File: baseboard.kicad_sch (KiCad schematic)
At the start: 45 parts, among them J10 AS7265X, J11 TFT_LCD2, J12 SERVO1, J13 USER_GPIO, J14 TFT_LCD, J15 SERVO2, J16 FAN, J17 ADC_IN, J5 Screw_Terminal_01x04, J6 DCMI_CAMERA, J7 LCD_CHAR, J8 UART1, J9 UART2, Q1 BCP56, Q2 BCP56, Q3 BCP56, U2 LM2676S-5, U3 AMS1117-3.3

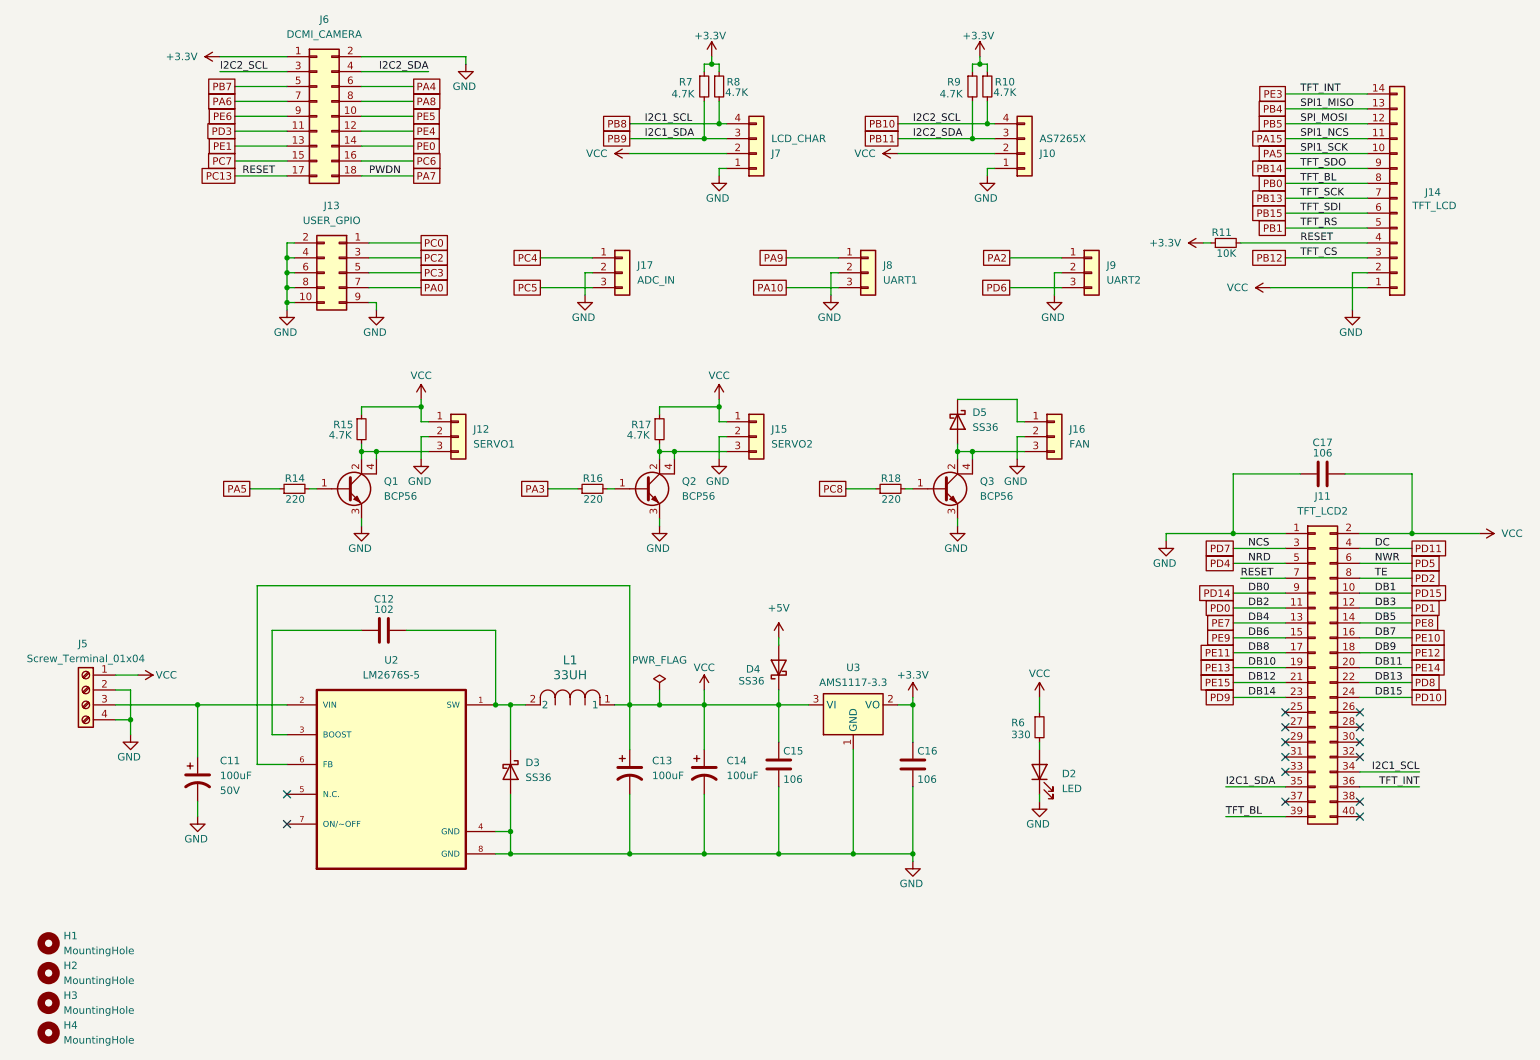
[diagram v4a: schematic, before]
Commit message: flipped camera connector
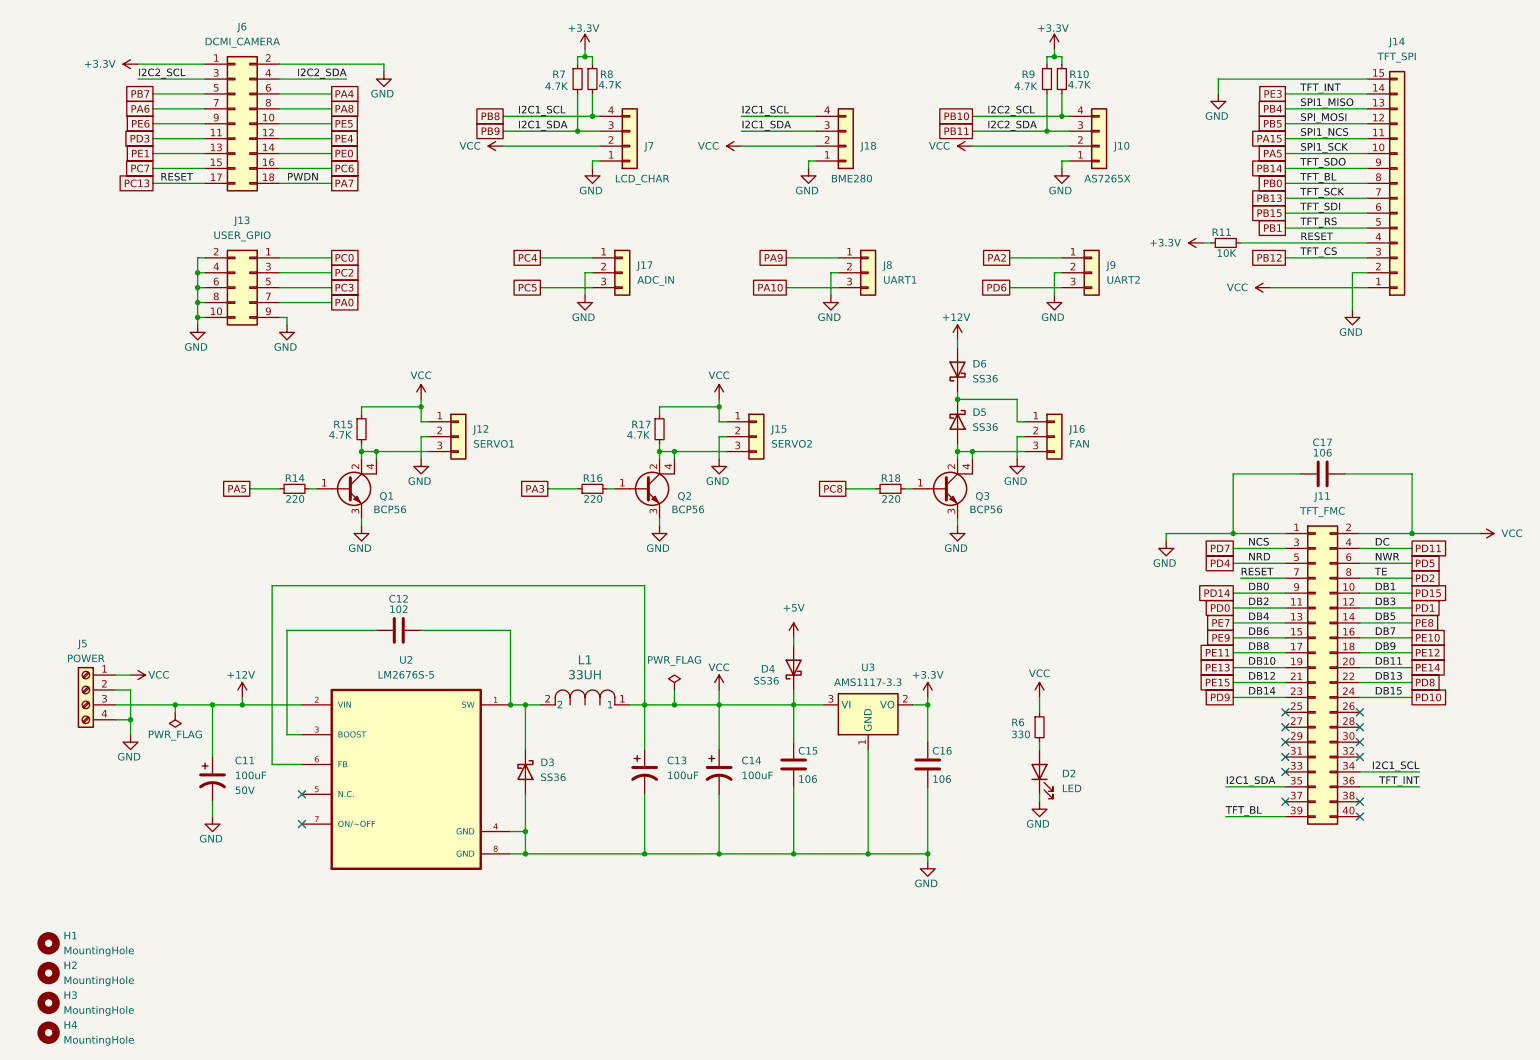
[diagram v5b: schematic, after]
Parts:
- removed J14: TFT_LCD, Connector_PinHeader_2.54mm:PinHeader_1x14_P2.54mm_Vertical, symbol LM2676S-3.3_NOPB:Conn_01x14
- added D6: SS36, Diode_SMD:D_SMA, symbol LM2676S-3.3_NOPB:SS36
- added J14: TFT_SPI, Connector_PinHeader_2.54mm:PinHeader_1x15_P2.54mm_Vertical, symbol Connector_Generic:Conn_01x15
- added J18: BME280, Connector_PinHeader_2.54mm:PinHeader_1x04_P2.54mm_Vertical, symbol LM2676S-3.3_NOPB:Conn_01x04
- D2: footprint LED_THT:LED_D3.0mm -> LED_SMD:LED_0805_2012Metric_Pad1.15x1.40mm_HandSolder
- J11: value TFT_LCD2 -> TFT_FMC
- J5: value Screw_Terminal_01x04 -> POWER
- J6: footprint Connector_PinHeader_2.54mm:PinHeader_2x09_P2.54mm_Vertical -> Connector_PinSocket_2.54mm:PinSocket_2x09_P2.54mm_Vertical
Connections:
- net GND: now also J14.15 (Pin_15), J14.2 (Pin_2), J18.1 (Pin_1)
- net PA15: now also J14.11 (Pin_11)
- net PA5: now also J14.10 (Pin_10)
- net PB0: now also J14.8 (Pin_8)
- net PB1: now also J14.5 (Pin_5)
- net PB12: now also J14.3 (Pin_3)
- net PB13: now also J14.7 (Pin_7)
- net PB14: now also J14.9 (Pin_9)
- net PB15: now also J14.6 (Pin_6)
- net PB4: now also J14.13 (Pin_13)
- net PB5: now also J14.12 (Pin_12)
- net PB8: now also J18.4 (Pin_4)
- net PB9: now also J18.3 (Pin_3)
- net PC13: now also J14.4 (Pin_4)
- net PE3: now also J14.14 (Pin_14)
- net VCC: now also J14.1 (Pin_1), J18.2 (Pin_2)
- net +12V: now reaches C11.1, J5.3 (Pin_3), U2.2 (VIN)
- net +12V: now also D6.2 (A)
- net at D5.1 (K), J16.1 (Pin_1): now also D6.1 (K)
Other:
- moved on the sheet: C11, C12, C13, C14, C15, C16, D3, D4, J10, J13, J6, J7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

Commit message: snapshot
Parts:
- removed H1, H2, H3, H4: MountingHole, MountingHole:MountingHole_3.2mm_M3, symbol LM2676S-3.3_NOPB:MountingHole
- removed Q1, Q2, Q3: BCP56, Package_TO_SOT_SMD:SOT-223-3_TabPin2, symbol Transistor_BJT:BCP56
- added H1, H2, H3, H4: ~, PCM_JLCPCB:Hole, 3mm, symbol PCM_JLCPCB-Manufacturing:Mounting Hole, 3mm, Via Stiched
- added Q1, Q2, Q3: BCP56, PCM_Package_TO_SOT_SMD_AKL:SOT-223-3_TabPin2, symbol PCM_Transistor_BJT_AKL:BCP56
- L1: footprint Inductor_SMD:L_Bourns-SRN8040_8x8.15mm -> JLCPCB:L_SMD,8x8mm
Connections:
- net GND: now also H1.1, H2.1, H3.1, H4.1, Q1.3 (E), Q2.3 (E), Q3.3 (E)
- net at J15.3 (Pin_3), R17.2: now also Q2.2 (C)
- net at D5.2 (A), J16.3 (Pin_3): now also Q3.2 (C)
- net at J12.3 (Pin_3), R15.2: now also Q1.2 (C)
- net at R14.2: now also Q1.1 (B)
- net at R18.2: now also Q3.1 (B)
- net at R16.2: now also Q2.1 (B)

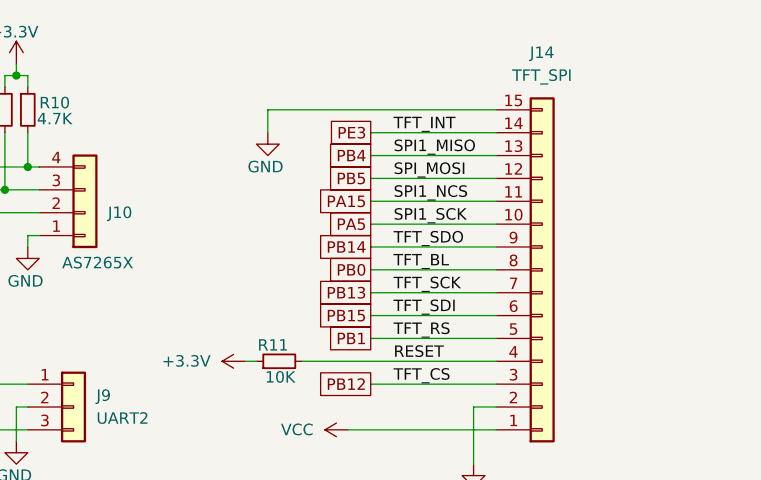
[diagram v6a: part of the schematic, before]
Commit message: Reassign pin (PA5 to PB3) to dix duplicate PA5
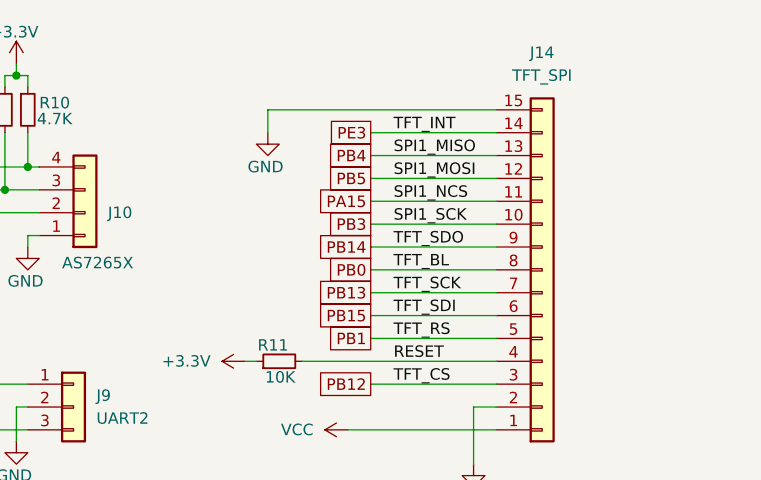
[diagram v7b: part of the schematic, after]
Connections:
- net PA5: no longer J14.10 (Pin_10)
- new net PB3: J14.10 (Pin_10)
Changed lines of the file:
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@@
 		)
 	)
-	(label "SPI_MOSI"
+	(label "SPI1_MOSI"
 		(at 232.41 36.83 0)
 		(effects
@@
 		)
 	)
-	(global_label "PA5"
+	(global_label "PB3"
 		(shape passive)
 		(at 229.87 41.91 180)
